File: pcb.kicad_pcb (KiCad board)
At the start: 2 copper layers, 100 x 100 mm, 14 parts, among them U1 ESP32-S3, U2 MPU-6050, U3 AMS1117-3.3V

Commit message: Design: Clean production ready flight controller layout asset deployment
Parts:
- removed ? (x4): , MountingHole:MountingHole_3.2mm_M3
- removed C1, C2: , Capacitor_SMD:C_0805_2012Metric
- removed D1, D2: , LED_SMD:LED_0805_2012Metric
- removed J1: , Connector_BarrelJack:BarrelJack_Horizontal
- removed R1, R2: , Resistor_SMD:R_0805_2012Metric
- removed U3: AMS1117-3.3V, Package_TO_SOT_SMD:SOT-223-3_TabPin2
- U1: value ESP32-S3 -> ESP32-S3-WROOM-1
- moved U2 10.0 mm to (120.0, 100.0)
- moved U1 5.00 mm to (80.0, 100.0)
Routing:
- net 0: track 104.0 -> 0.00 mm
- net (no net): track 0.00 -> 94.0 mm
- net 1: track 61.0 -> 0.00 mm
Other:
- board text removed: "AEROFORM AVIONICS FLIGHT CONTROLLER"
- board text removed: "DESIGNED VIA AUTOMATED PYTHON ENGINE"
- board text removed: "POWER BUS ACTIVE"

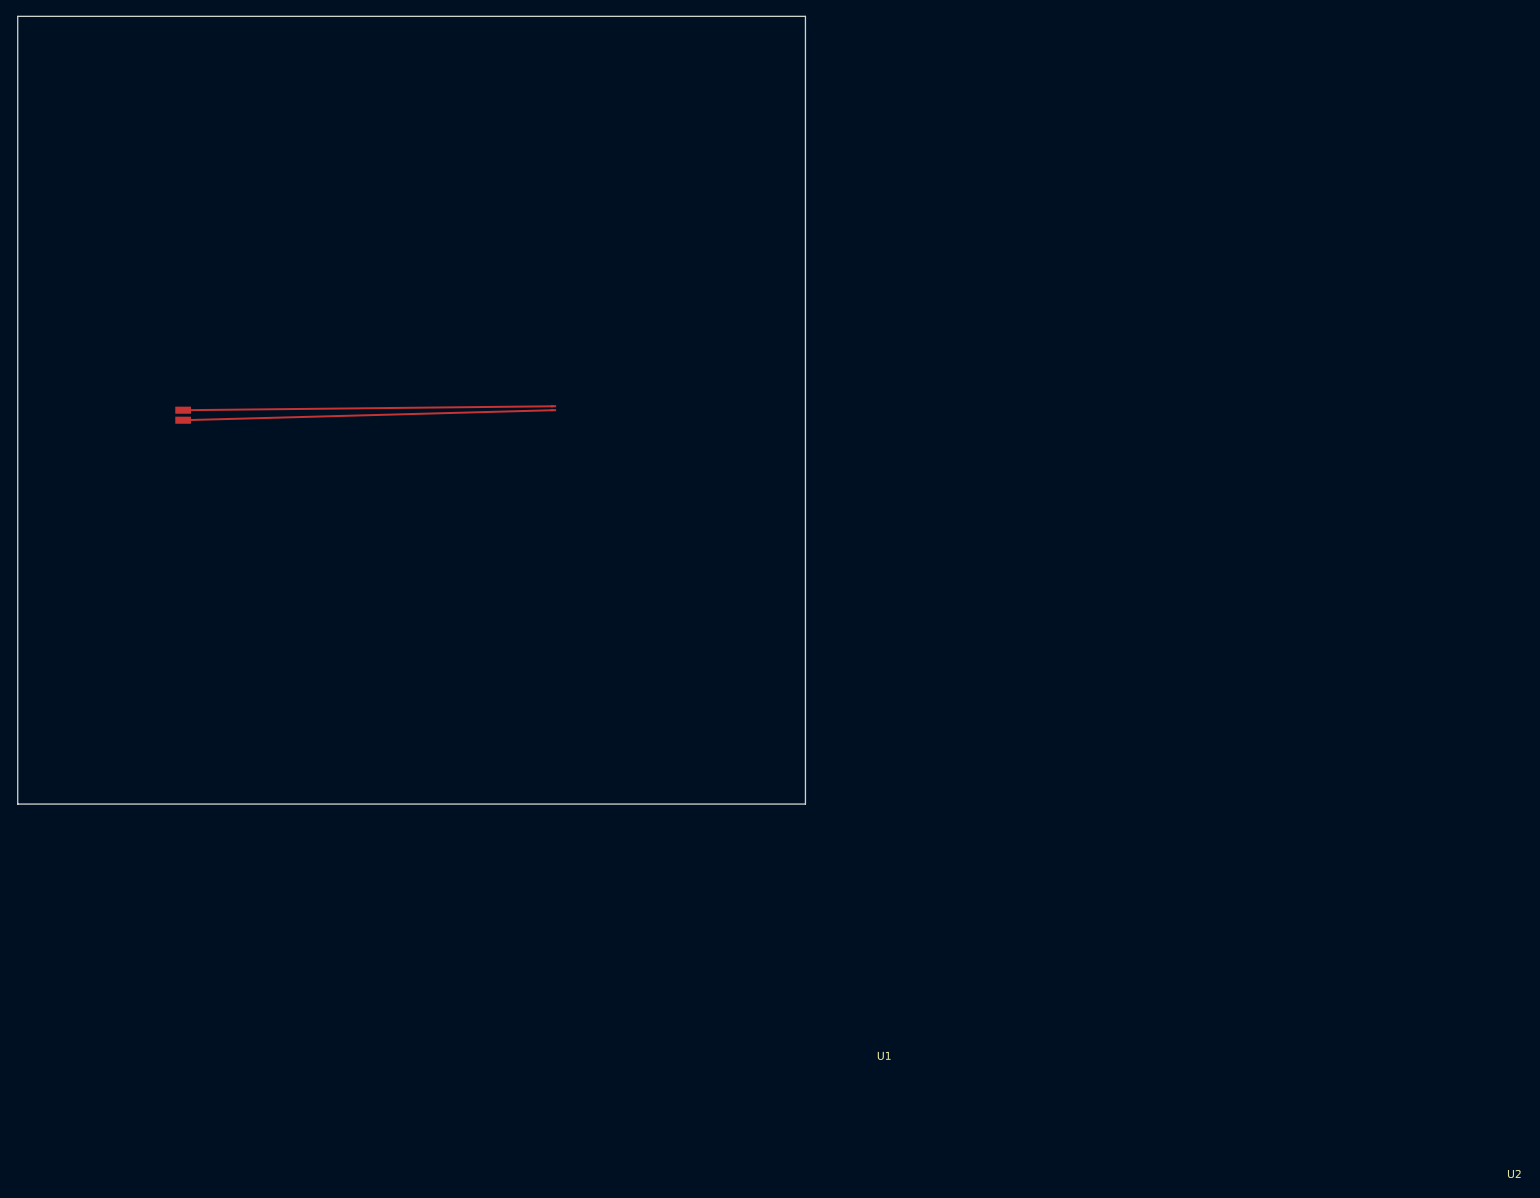
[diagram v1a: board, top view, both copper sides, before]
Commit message: Fix: Overwrite file with complete interactive circuit design layout
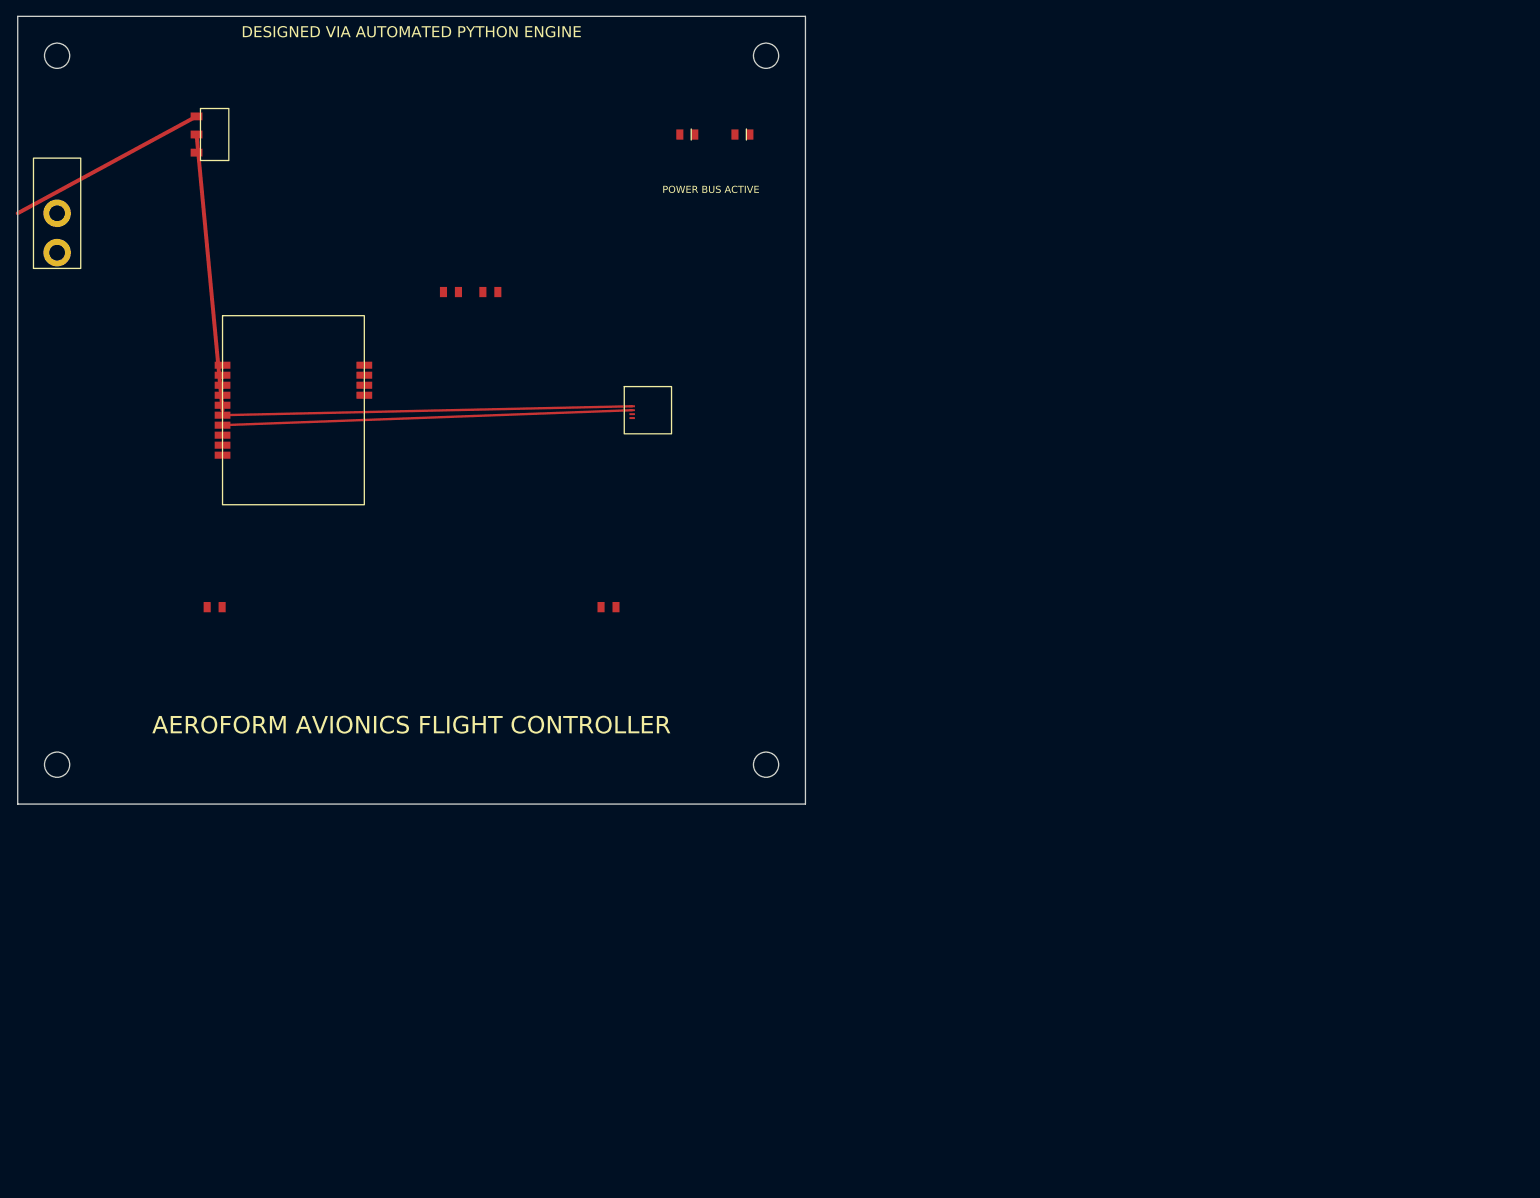
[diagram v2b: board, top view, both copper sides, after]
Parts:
- added ?: , MountingHole:MountingHole_3.2mm_M3, F.Cu at (55.0, 55.0)
- added ?: , MountingHole:MountingHole_3.2mm_M3, F.Cu at (145.0, 55.0)
- added ?: , MountingHole:MountingHole_3.2mm_M3, F.Cu at (145.0, 145.0)
- added ?: , MountingHole:MountingHole_3.2mm_M3, F.Cu at (55.0, 145.0)
- added C1: , Capacitor_SMD:C_0805_2012Metric, F.Cu at (75.0, 125.0)
- added C2: , Capacitor_SMD:C_0805_2012Metric, F.Cu at (125.0, 125.0)
- added D1: , LED_SMD:LED_0805_2012Metric, F.Cu at (135.0, 65.0)
- added D2: , LED_SMD:LED_0805_2012Metric, F.Cu at (142.0, 65.0)
- added J1: , Connector_BarrelJack:BarrelJack_Horizontal, F.Cu at (55.0, 75.0)
- added R1: , Resistor_SMD:R_0805_2012Metric, F.Cu at (105.0, 85.0)
- added R2: , Resistor_SMD:R_0805_2012Metric, F.Cu at (110.0, 85.0)
- added U3: AMS1117-3.3V, Package_TO_SOT_SMD:SOT-223-3_TabPin2, F.Cu at (75.0, 65.0)
- U1: value ESP32-S3-WROOM-1 -> ESP32-S3
- moved U2 10.0 mm to (130.0, 100.0)
- moved U1 5.00 mm to (85.0, 100.0)
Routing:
- net 0: track 0.00 -> 104.0 mm
- net (no net): track 94.0 -> 0.00 mm
- net 1: track 0.00 -> 61.0 mm
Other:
- board text added: "AEROFORM AVIONICS FLIGHT CONTROLLER"
- board text added: "DESIGNED VIA AUTOMATED PYTHON ENGINE"
- board text added: "POWER BUS ACTIVE"
